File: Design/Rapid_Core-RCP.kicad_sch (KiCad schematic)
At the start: 58 parts, among them IC1 TLIN1039DDFRQ1, IC2 TLIN1039DDFRQ1, IC3 SHT30A-DIS-B2.5KS, J1 CMD PIN, J2 CMD PIN, J3 LIN_1, J4 LIN_2, J5 GPIO_CONN_x_4, J6 SWD_Debug, J7 SPI_CONN, J8 USART, SW1 SW_Push, U1 STM32F446RETx, Y1 8_MHz, Y2 32.768_KHz

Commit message: Schematic Design complete
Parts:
- removed R11, R12, R13, R14: R, symbol Device:R
- added FID1, FID2, FID3, FID4: Fiducial, Fiducial:Fiducial_1.5mm_Mask3mm, symbol Mechanical:Fiducial
- added H1, H2, H3, H4: MountingHole_Pad, MountingHole:MountingHole_2.2mm_M2_Pad, symbol Mechanical:MountingHole_Pad
- added TP13 (x20): TestPoint, TestPoint:TestPoint_Pad_D2.5mm, symbol Connector:TestPoint
- C17: footprint (none) -> Capacitor_SMD:C_0805_2012Metric_Pad1.18x1.45mm_HandSolder
- FB1: footprint (none) -> Inductor_SMD:L_0805_2012Metric_Pad1.05x1.20mm_HandSolder
- J1: footprint (none) -> Connector_PinHeader_2.54mm:PinHeader_1x02_P2.54mm_Vertical
- J3, J4: footprint (none) -> TerminalBlock_Phoenix:TerminalBlock_Phoenix_MKDS-1,5-2_1x02_P5.00mm_Horizontal
- SW1: footprint (none) -> Button_Switch_SMD:SW_SPST_CK_RS282G05A3
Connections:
- net +3.3V: now also TP13.1, TP13.1
- net GND1: now also H1.1, H2.1, H3.1, H4.1
- net I2C_SCL_HUM: now also TP13.1
- net I2C_SDA_HUM: now also TP13.1
- net LIN1: now also TP13.1
- net LIN1_EN: now also U1.50 (PA15), TP13.1
- net LIN1_RX: now also TP13.1
- net LIN1_TX: now also U1.51 (PC10), TP13.1
- net LIN2: now also TP13.1
- net LIN2_EN: now also U1.55 (PB3), TP13.1
- net LIN2_RX: now also TP13.1
- net LIN2_TX: now also U1.53 (PC12), TP13.1
- net SPI1_MISO: now also TP13.1
- net SPI1_MOSI: now also TP13.1
- net SPI1_SCK: now also TP13.1
- net SPI2_MISO: now also TP13.1
- net SPI2_MOSI: now also TP13.1
- net SPI2_SCK: now also TP13.1
- net USART2_RX: now also TP13.1
- net USART2_TX: now also TP13.1
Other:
- note added: "C17 : C0805C475K9RAC7800"
- moved on the sheet: C10, C9, J3

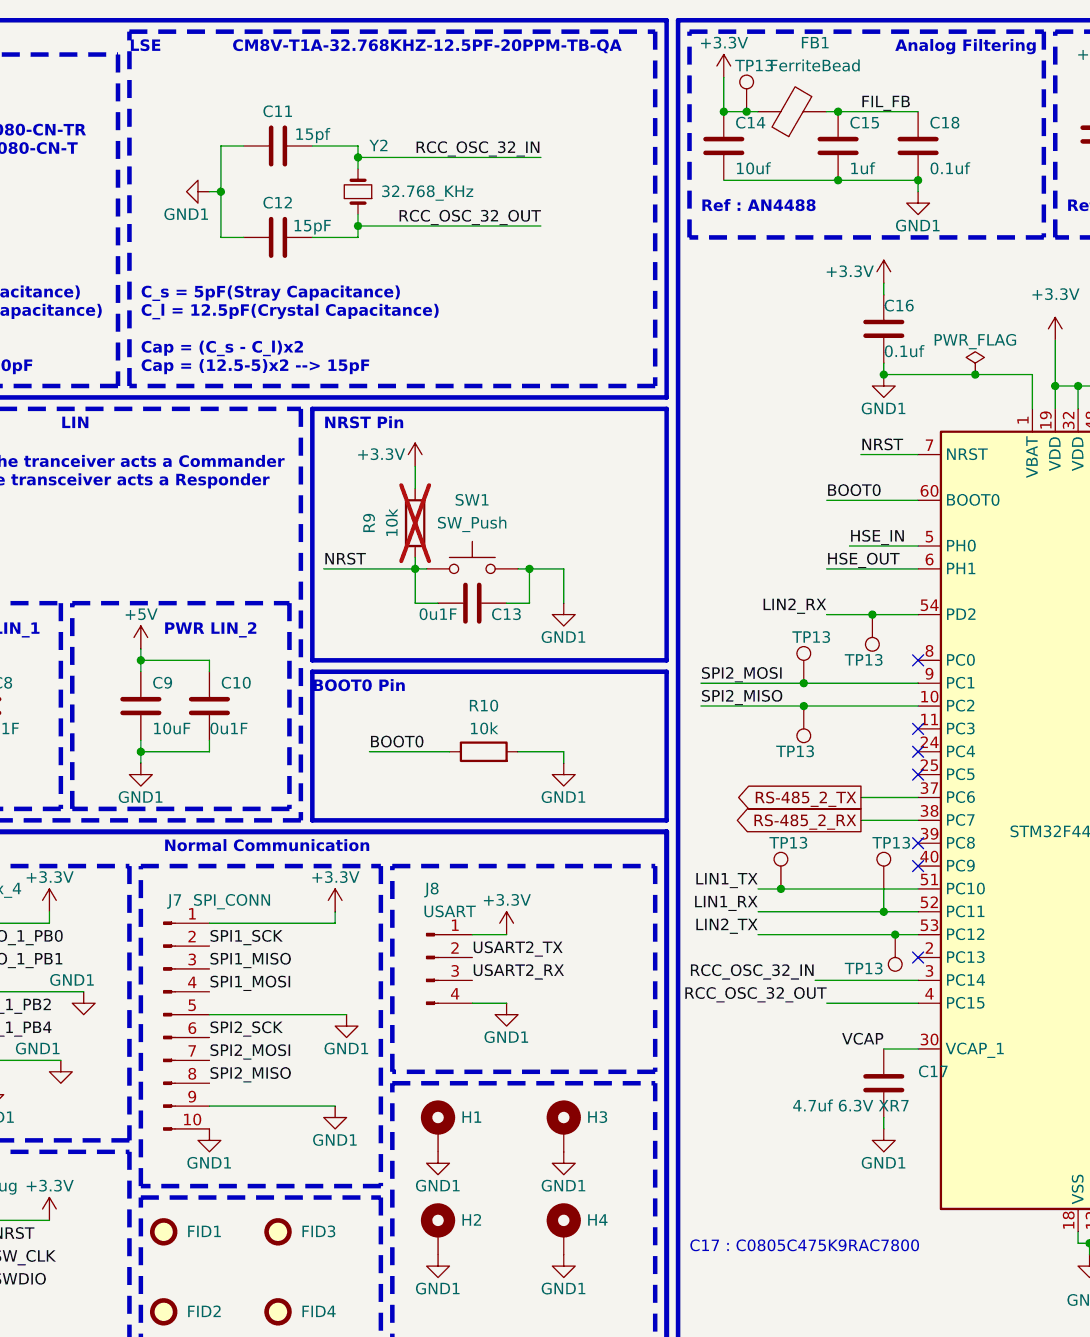
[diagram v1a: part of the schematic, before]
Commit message: PCB design started, comps arranged
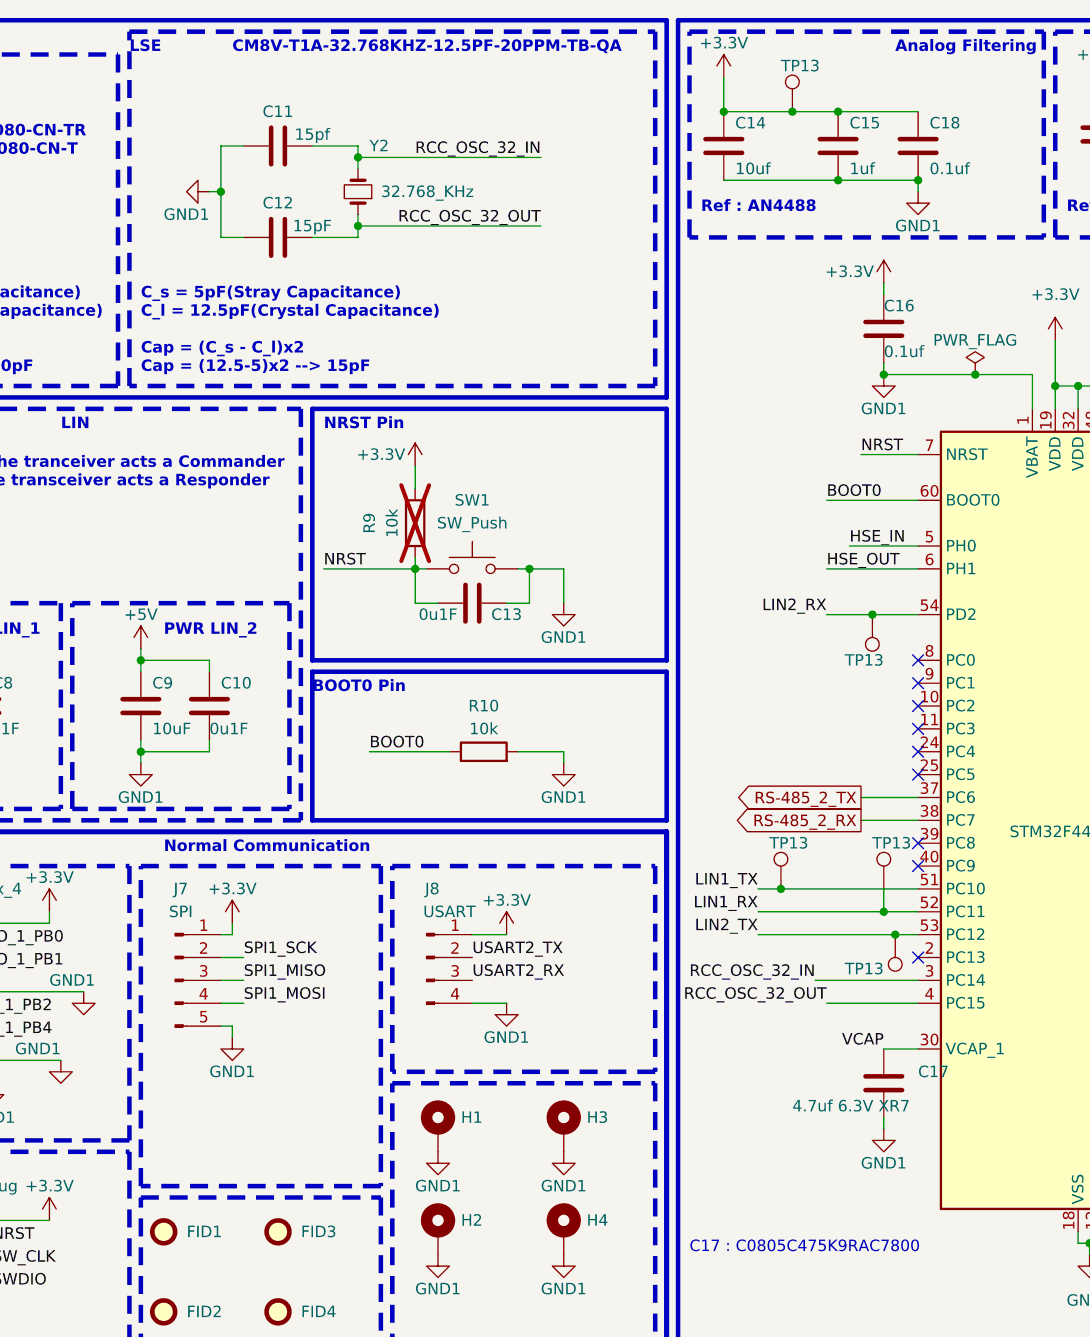
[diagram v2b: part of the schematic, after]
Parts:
- removed FB1: FerriteBead, Inductor_SMD:L_0805_2012Metric_Pad1.05x1.20mm_HandSolder, symbol Device:FerriteBead
- removed J7: SPI_CONN, Connector_PinHeader_2.54mm:PinHeader_1x10_P2.54mm_Vertical, symbol Connector:Conn_01x10_Pin
- removed TP13 (x2): TestPoint, TestPoint:TestPoint_Pad_D2.5mm, symbol Connector:TestPoint
- added J7: SPI, Connector_PinHeader_2.54mm:PinHeader_1x05_P2.54mm_Vertical, symbol Connector:Conn_01x05_Pin
- TP13: footprint TestPoint:TestPoint_Pad_D2.5mm -> TestPoint:TestPoint_Pad_D1.0mm
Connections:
- net FIL_FB is gone; now on net +3.3V: C15.1, C18.1
- net +3.3V: now also J7.1 (Pin_1)
- net GND1: now also J7.5 (Pin_5)
- net SPI1_MISO: now also J7.3 (Pin_3)
- net SPI1_MOSI: now also J7.4 (Pin_4)
- net SPI1_SCK: now also J7.2 (Pin_2)
- net SPI2_MISO: no longer names the net of U1.10 (PC2)
- net SPI2_MOSI: no longer names the net of U1.9 (PC1)
- no-connect marks 18 -> 20
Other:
- moved on the sheet: TP13

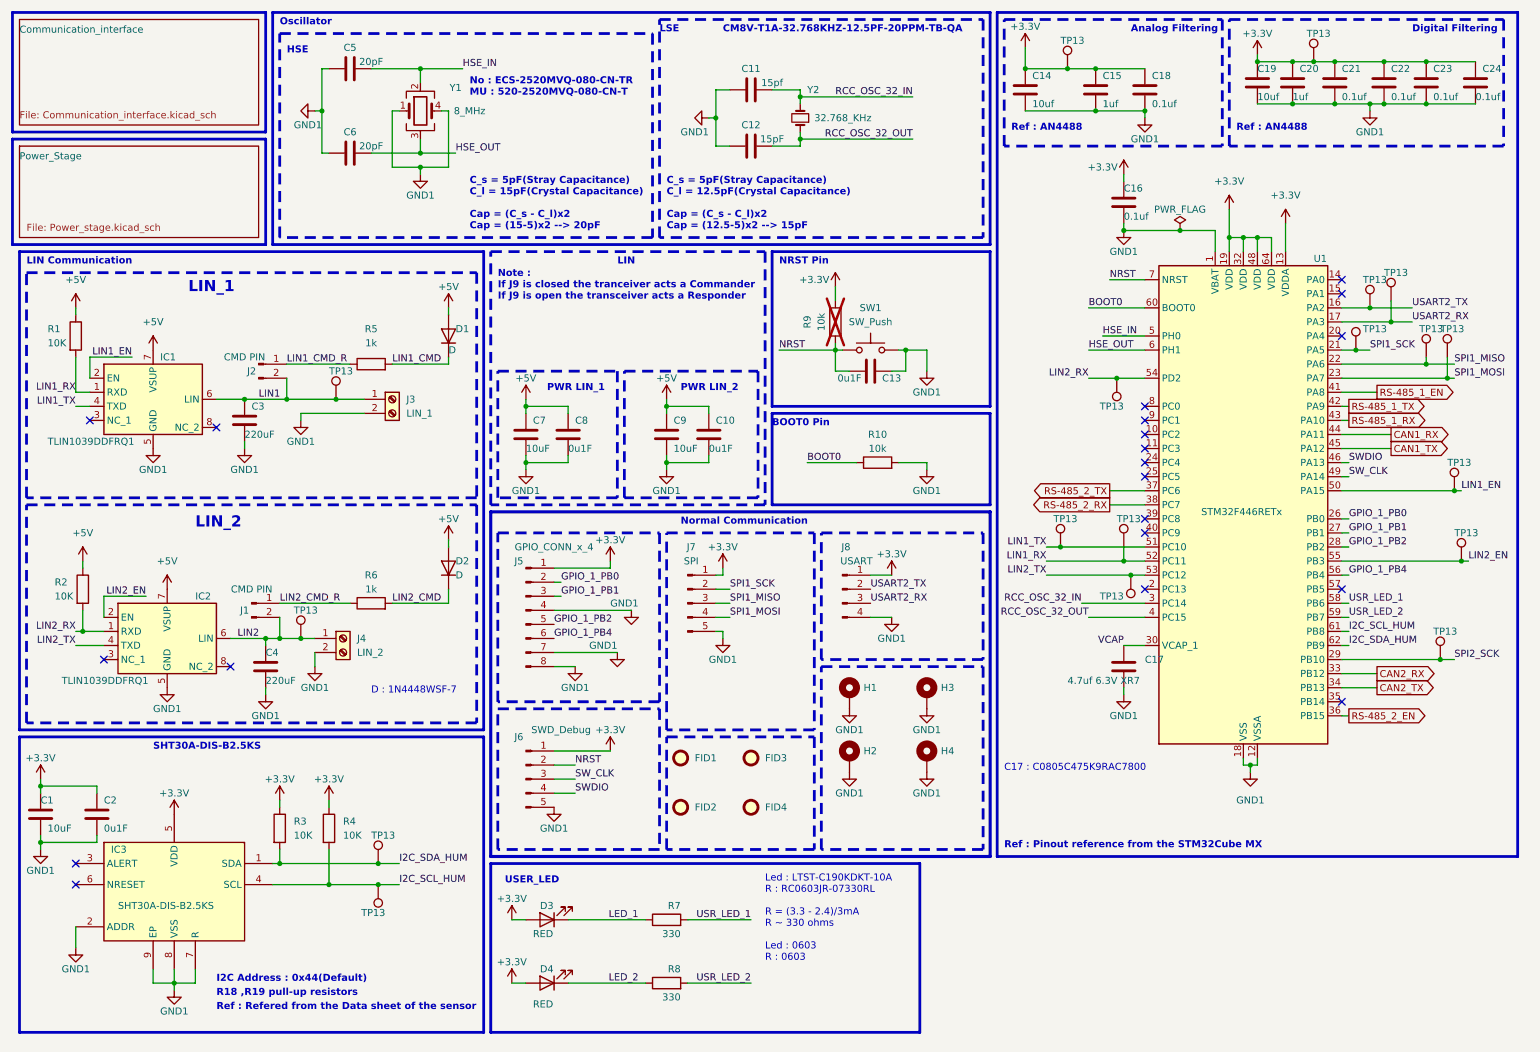
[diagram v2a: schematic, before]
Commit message: Temp complete of communication section , added Safety caps
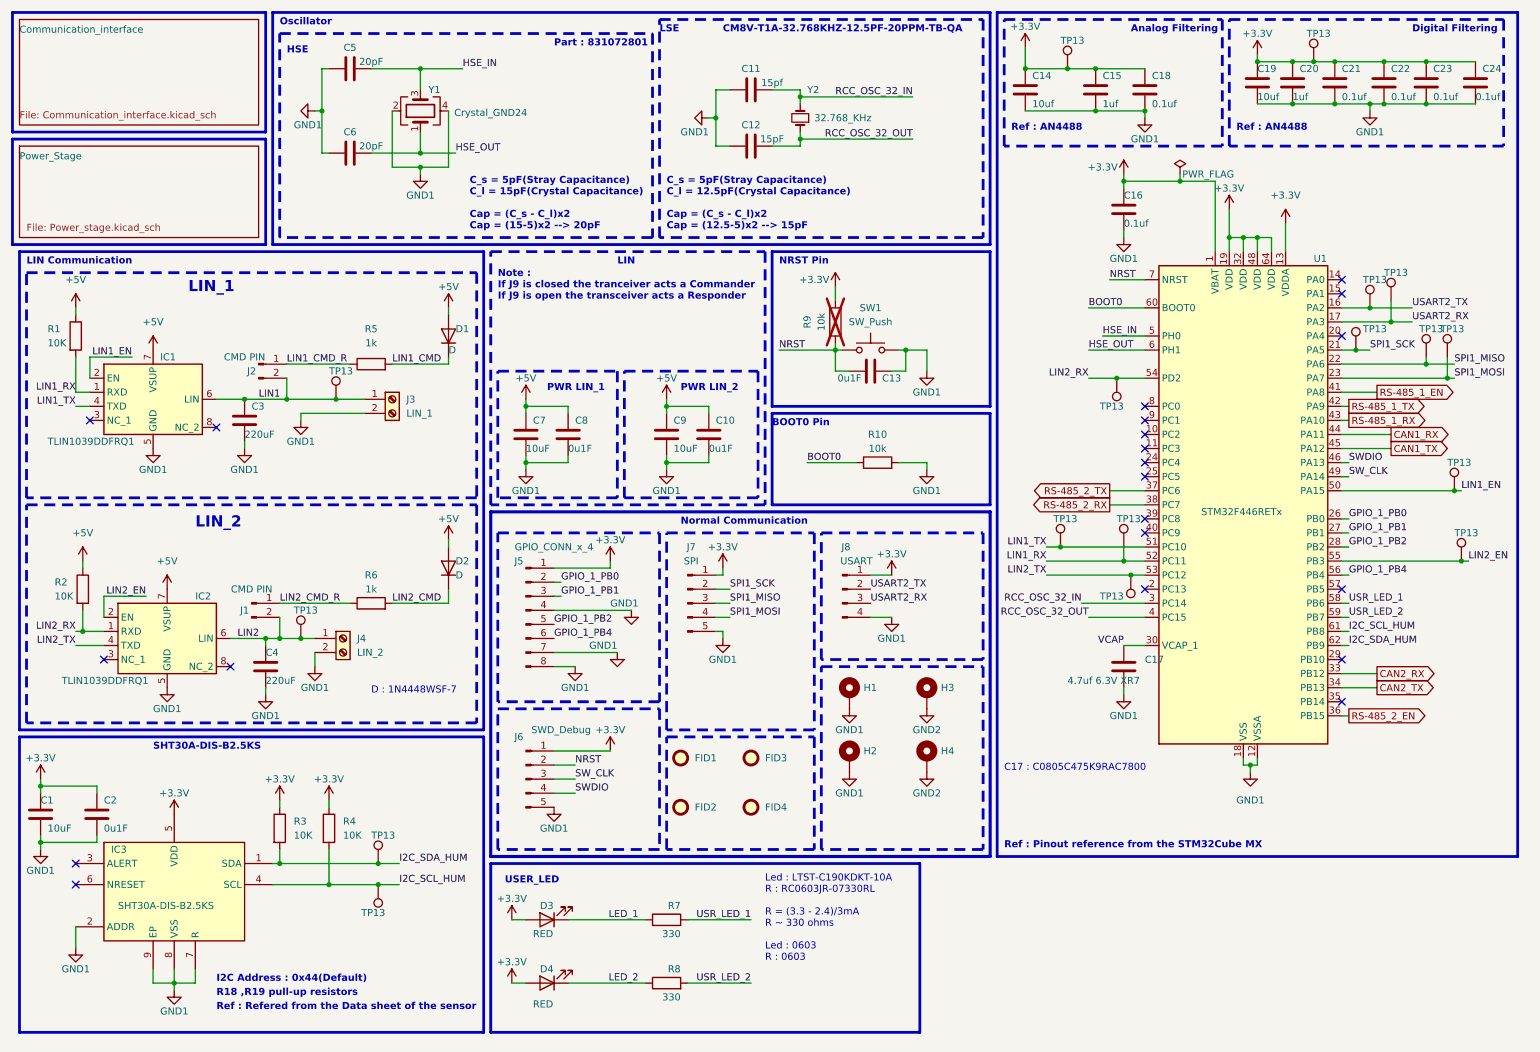
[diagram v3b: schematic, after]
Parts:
- removed TP13: TestPoint, TestPoint:TestPoint_Pad_D1.0mm, symbol Connector:TestPoint
- removed Y1: 8_MHz, ECS-2520MVLC_8MHz:ECS2520MVLC080BNTR, symbol Device:Crystal_GND23
- added Y1: Crystal_GND24, Crystal:Crystal_SMD_2520-4Pin_2.5x2.0mm, symbol Device:Crystal_GND24
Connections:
- net +3.3V: now also U1.1 (VBAT)
- net GND1: now also Y1.2, Y1.4; no longer H3.1, H4.1, U1.1 (VBAT)
- net HSE_IN: now also Y1.3
- net HSE_OUT: now also Y1.1
- net SPI2_SCK: no longer names the net of U1.29 (PB10)
- new net GND2: H3.1, H4.1
- no-connect marks 20 -> 21
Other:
- note added: "Part : 831072801"
- note removed: "No : ECS-2520MVQ-080-CN-TR MU : 520-2520MVQ-080-CN-T"
- moved on the sheet: C16

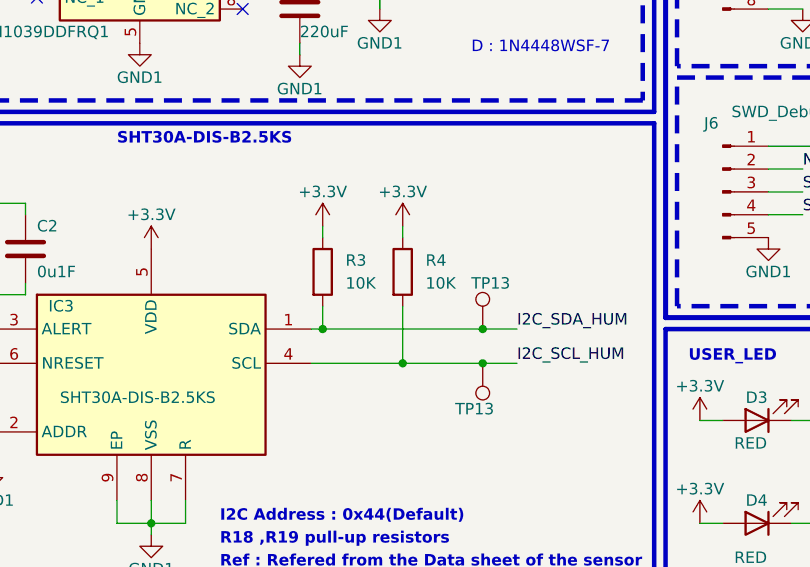
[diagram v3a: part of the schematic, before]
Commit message: value changed for I2C pullup
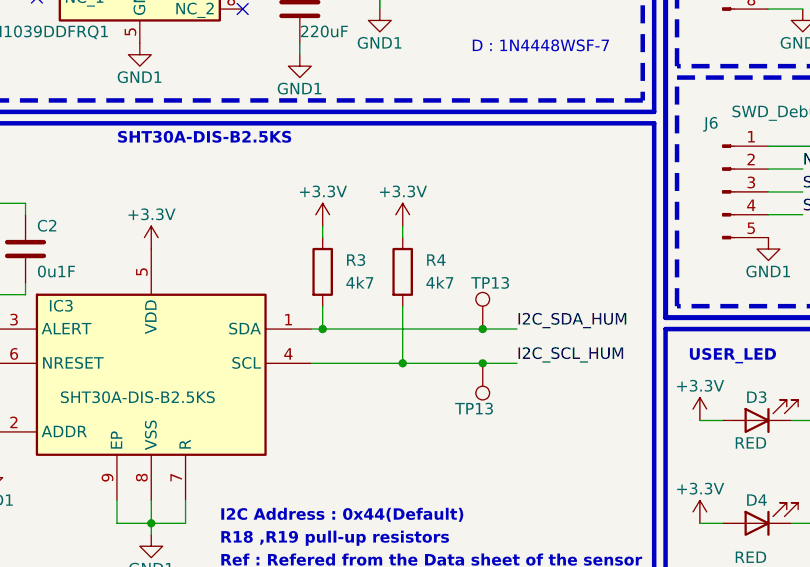
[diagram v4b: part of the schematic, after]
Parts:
- R3, R4: value 10K -> 4k7
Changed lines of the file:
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@@
       (effects (font (size 1.27 1.27)) (justify left))
     )
-    (property "Value" "10K" (at 63.5 161.29 0)
+    (property "Value" "4k7" (at 63.5 161.29 0)
       (effects (font (size 1.27 1.27)) (justify left))
     )
@@
       (effects (font (size 1.27 1.27)) (justify left))
     )
-    (property "Value" "10K" (at 72.39 161.29 0)
-      (effects (font (size 1.27 1.27)) (justify left))
-    )
+    (property "Value" "4k7" (at 72.39 161.29 0)
+      (effects (font (size 1.27 1.27)) (justify left))
+    )

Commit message: Added all the sections
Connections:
- net NRST: now also J6.3 (Pin_3); no longer J6.2 (Pin_2)
- net SW_CLK: now also J6.2 (Pin_2); no longer J6.3 (Pin_3)
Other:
- note added: "R3 ,R4 pull-up resistors"
- note removed: "R18 ,R19 pull-up resistors"
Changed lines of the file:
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@@
-    (stroke (width 0) (type default))
-  )
-  (wire (pts (xy 110.49 151.13) (xy 114.3 151.13))
     (stroke (width 0) (type default))
   )
@@
   )
   (wire (pts (xy 254 139.7) (xy 252.73 139.7))
-    (stroke (width 0) (type default))
-  )
-  (wire (pts (xy 114.3 148.59) (xy 110.49 148.59))
     (stroke (width 0) (type default))
   )
@@
   (text "Led : LTST-C190KDKT-10A\nR : RC0603JR-07330RL\n\nR = (3.3 - 2.4)/3mA \nR ~ 330 ohms\n\nLed : 0603\nR : 0603\n"
     (at 148.59 184.15 0)
-    (effects (font (size 1.27 1.27)) (justify left bottom))
+    (effects (font (size 1.27 1.27) (thickness 0.254) bold) (justify left bottom))
   )
   (text "LIN_1\n" (at 44.45 63.5 0)
@@
     (effects (font (size 1.27 1.27) bold) (justify left bottom))
   )
-  (text "C17 : C0805C475K9RAC7800" (at 191.77 149.86 0)
-    (effects (font (size 1.27 1.27)) (justify left bottom))
+  (text "C17 : C0805C475K9RAC7800" (at 191.77 160.02 0)
+    (effects (font (size 1.27 1.27) (thickness 0.254) bold) (justify left bottom))
   )
   (text "Note :\nIf J9 is closed the tranceiver acts a Commander\nIf J9 is open the transceiver acts a Responder"
@@
   )
   (text "D : 1N4448WSF-7" (at 77.47 135.89 0)
-    (effects (font (size 1.27 1.27)) (justify left bottom))
+    (effects (font (size 1.27 1.27) (thickness 0.254) bold) (justify left bottom))
   )
   (text "LIN_2\n\n" (at 45.72 109.22 0)
@@
     (effects (font (size 1.27 1.27) bold) (justify left bottom))
   )
-  (text "R18 ,R19 pull-up resistors  " (at 49.53 190.5 0)
+  (text "R3 ,R4 pull-up resistors  " (at 49.53 190.5 0)
     (effects (font (size 1.27 1.27) bold) (justify left bottom))
   )
@@
     (effects (font (size 1.27 1.27)) (justify left bottom))
   )
-  (label "NRST" (at 114.3 148.59 0) (fields_autoplaced)
+  (label "NRST" (at 110.49 151.13 0) (fields_autoplaced)
     (effects (font (size 1.27 1.27)) (justify left bottom))
   )
@@
     (effects (font (size 1.27 1.27)) (justify left bottom))
   )
-  (label "SW_CLK" (at 114.3 151.13 0) (fields_autoplaced)
+  (label "SW_CLK" (at 110.49 148.59 0) (fields_autoplaced)
     (effects (font (size 1.27 1.27)) (justify left bottom))
   )
@@
   (symbol (lib_id "Device:C") (at 213.36 130.81 0) (unit 1)
     (in_bom yes) (on_board yes) (dnp no)
-    (property "Reference" "C17" (at 217.17 129.54 0)
-      (effects (font (size 1.27 1.27)) (justify left))
-    )
+    (property "Reference" "C17" (at 208.28 128.27 0)
+      (effects (font (size 1.27 1.27)) (justify left))
+    )
